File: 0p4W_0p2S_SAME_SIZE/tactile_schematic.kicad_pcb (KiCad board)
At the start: 2 copper layers, 109.6 x 67.4 mm, 55 parts, among them IC1 CY8C4145PVI-PS431, J1 Conn_01x03, J2 Conn_01x04, J3 Conn_01x04, J4 Conn_01x03, J5 Conn_ARM_SWD_TagConnect_TC203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

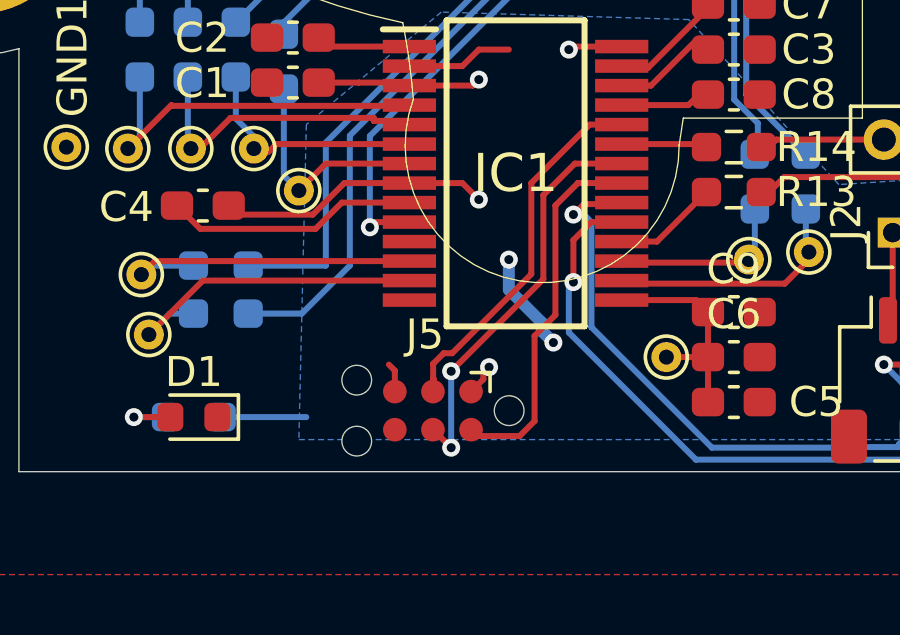
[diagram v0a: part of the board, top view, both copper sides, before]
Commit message: move prog connector up, make bottom of gnd plane connected propelrly
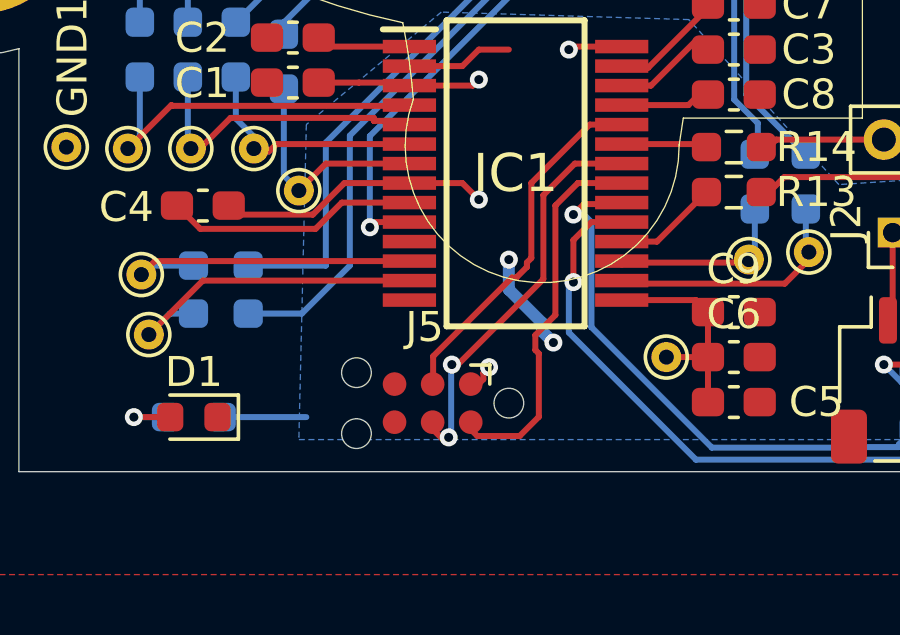
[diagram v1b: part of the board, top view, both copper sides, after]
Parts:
- moved J5 0.25 mm to (183.5, 85.8)
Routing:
- net GND: track 25.4 -> 24.4 mm
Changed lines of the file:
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@@
 	(footprint "Connector:Tag-Connect_TC2030-IDC-NL_2x03_P1.27mm_Vertical"
 		(layer "F.Cu")
-		(at 183.47 86.035 180)
+		(at 183.46 85.785 180)
 		(descr "Tag-Connect programming header; http://www.tag-connect.com/Materials/TC2030-IDC-NL.pdf")
 		(tags "tag connect programming header pogo pins")
@@
 			(polygon
 				(pts
-					(xy 182.2 86.67) (xy 184.74 86.67) (xy 184.74 85.4) (xy 182.2 85.4)
+					(xy 182.19 86.42) (xy 184.73 86.42) (xy 184.73 85.15) (xy 182.19 85.15)
 				)
 			)
@@
 	)
 	(segment
-		(start 182.2 84.7)
-		(end 182 84.5)
-		(width 0.2)
-		(layer "F.Cu")
-		(net 2)
-	)
-	(segment
 		(start 180.432786 79.1)
 		(end 179.556786 79.976)
@@
 		(net 2)
 	)
-	(segment
-		(start 182.2 85.4)
-		(end 182.2 84.7)
-		(width 0.2)
-		(layer "F.Cu")
-		(net 2)
-	)
 	(via
 		(at 186 81)
@@
 	)
 	(segment
-		(start 183.477687 86.67)
-		(end 184.07737 87.269683)
+		(start 183.84112 87.033433)
+		(end 183.477687 86.67)
 		(width 0.2)
 		(layer "F.Cu")
@@
 	)
 	(segment
-		(start 188.2 77.8)
-		(end 189.761505 77.8)
+		(start 183.886427 87.033433)
+		(end 183.84112 87.033433)
 		(width 0.2)
 		(layer "F.Cu")
@@
 	)
 	(segment
+		(start 183.993552 86.926308)
+		(end 183.886427 87.033433)
+		(width 0.2)
+		(layer "F.Cu")
+		(net 22)
+	)
+	(segment
+		(start 188.2 77.8)
+		(end 189.761505 77.8)
+		(width 0.2)
+		(layer "F.Cu")
+		(net 22)
+	)
+	(segment
+		(start 183.477687 86.67)
+		(end 183.47 86.67)
+		(width 0.2)
+		(layer "F.Cu")
+		(net 22)
+	)
+	(segment
 		(start 187.151 81.649)
 		(end 187.151 78.849)
@@
 	)
 	(segment
-		(start 184.07737 84.72263)
-		(end 187.151 81.649)
+		(start 184.1 84.5)
+		(end 184.3 84.5)
 		(width 0.2)
 		(layer "F.Cu")
@@
 	)
 	(segment
-		(start 183.47 86.67)
-		(end 183.477687 86.67)
+		(start 184.3 84.5)
+		(end 187.151 81.649)
 		(width 0.2)
 		(layer "F.Cu")
@@
 	)
 	(via
-		(at 184.07737 87.269683)
+		(at 183.993552 86.926308)
 		(size 0.6)
 		(drill 0.3)
@@
 	)
 	(via
-		(at 184.07737 84.72263)
+		(at 184.1 84.5)
 		(size 0.6)
 		(drill 0.3)
@@
 	)
 	(segment
-		(start 184.07737 84.72263)
-		(end 184.07737 87.269683)
+		(start 184.065626 86.926308)
+		(end 183.993552 86.926308)
+		(width 0.2)
+		(layer "B.Cu")
+		(net 22)
+	)
+	(segment
+		(start 184.1 84.5)
+		(end 184.07737 84.52263)
+		(width 0.2)
+		(layer "B.Cu")
+		(net 22)
+	)
+	(segment
+		(start 184.07737 86.914564)
+		(end 184.065626 86.926308)
+		(width 0.2)
+		(layer "B.Cu")
+		(net 22)
+	)
+	(segment
+		(start 184.07737 84.52263)
+		(end 184.07737 86.914564)
 		(width 0.2)
 		(layer "B.Cu")
@@
 	)
 	(segment
-		(start 183.828427 84.12163)
-		(end 184.11127 84.12163)
+		(start 186.75 78.447005)
+		(end 188.697005 76.5)
 		(width 0.2)
 		(layer "F.Cu")
@@
 	)
 	(segment
-		(start 184.11127 84.12163)
-		(end 186.75 81.4829)
+		(start 186.099 81.601)
+		(end 186.248943 81.601)
 		(width 0.2)
 		(layer "F.Cu")
@@
 	)
 	(segment
-		(start 186.75 81.4829)
-		(end 186.75 78.447005)
+		(start 183.47637 84.22363)
+		(end 186.099 81.601)
 		(width 0.2)
 		(layer "F.Cu")
@@
 	)
 	(segment
-		(start 186.75 78.447005)
-		(end 188.697005 76.5)
+		(start 186.601 81.248943)
+		(end 186.601 81.099)
+		(width 0.2)
+		(layer "F.Cu")
+		(net 28)
+	)
+	(segment
+		(start 183.47637 84.971573)
+		(end 183.47637 84.22363)
+		(width 0.2)
+		(layer "F.Cu")
+		(net 28)
+	)
+	(segment
+		(start 186.75 80.95)
+		(end 186.75 78.447005)
 		(width 0.2)
 		(layer "F.Cu")
@@
 	)
 	(segment
-		(start 183.47637 84.473687)
-		(end 183.828427 84.12163)
+		(start 183.47 85.4)
+		(end 183.47 85.03)
 		(width 0.2)
 		(layer "F.Cu")
@@
 	)
 	(segment
-		(start 183.47637 84.971573)
-		(end 183.47637 84.473687)
+		(start 188.697005 76.5)
+		(end 189.761505 76.5)
 		(width 0.2)
 		(layer "F.Cu")
@@
 	)
 	(segment
-		(start 183.47 85.4)
-		(end 183.47 85.03)
+		(start 186.248943 81.601)
+		(end 186.601 81.248943)
 		(width 0.2)
 		(layer "F.Cu")
@@
 	)
 	(segment
-		(start 188.697005 76.5)
-		(end 189.761505 76.5)
+		(start 186.601 81.099)
+		(end 186.75 80.95)
 		(width 0.2)
 		(layer "F.Cu")
@@
 	)
 	(segment
-		(start 186.360549 86.8813)
-		(end 184.9513 86.8813)
+		(start 187 86.241849)
+		(end 186.360549 86.8813)
 		(width 0.2)
 		(layer "F.Cu")
@@
 	)
 	(segment
-		(start 186.8563 83.543756)
-		(end 186.8563 86.385549)
+		(start 186.360549 86.8813)
+		(end 184.9513 86.8813)
 		(width 0.2)
 		(layer "F.Cu")
@@
 	)
 	(segment
-		(start 188.3 78.45)
-		(end 187.552 79.198)
+		(start 186.883285 84.014658)
+		(end 187 84.131373)
 		(width 0.2)
 		(layer "F.Cu")
@@
 	)
 	(segment
-		(start 186.8563 86.385549)
-		(end 186.360549 86.8813)
+		(start 184.9513 86.8813)
+		(end 184.74 86.67)
 		(width 0.2)
 		(layer "F.Cu")
@@
 	)
 	(segment
-		(start 184.9513 86.8813)
-		(end 184.74 86.67)
+		(start 187.552 82.848057)
+		(end 186.883285 83.516772)
 		(width 0.2)
 		(layer "F.Cu")
@@
 	)
 	(segment
-		(start 187.552 82.848057)
-		(end 186.8563 83.543756)
+		(start 186.883285 83.516772)
+		(end 186.883285 84.014658)
 		(width 0.2)
 		(layer "F.Cu")
@@
 	)
 	(segment
+		(start 188.3 78.45)
+		(end 187.552 79.198)
+		(width 0.2)
+		(layer "F.Cu")
+		(net 32)
+	)
+	(segment
+		(start 187 84.131373)
+		(end 187 86.241849)
+		(width 0.2)
+		(layer "F.Cu")
+		(net 32)
+	)
+	(segment
 		(start 179.1 78.6)
 		(end 179.9 77.8)
@@
 		(hatch edge 0.5)
 		(connect_pads
-			(clearance 0.5)
+			(clearance 0.3)
 		)
-		(min_thickness 0.25)
+		(min_thickness 0.2)
 		(filled_areas_thickness no)
 		(fill yes
-			(thermal_gap 0.5)
+			(thermal_gap 0.4)
 			(thermal_bridge_width 0.5)
 		)
